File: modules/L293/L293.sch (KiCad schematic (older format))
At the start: 40 parts, among them J1 2, J10 11, J11 12, J12 13, J13 A0, J14 A1, J15 A2, J16 A3, J17 A4, J18 A5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

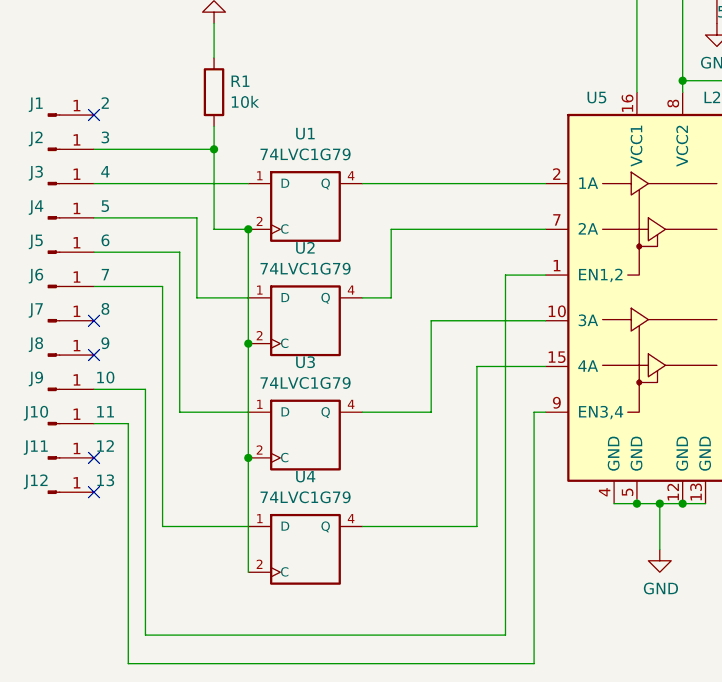
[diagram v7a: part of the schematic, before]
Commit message: Motor shield v2 in work Attention! Pin numbers changed!
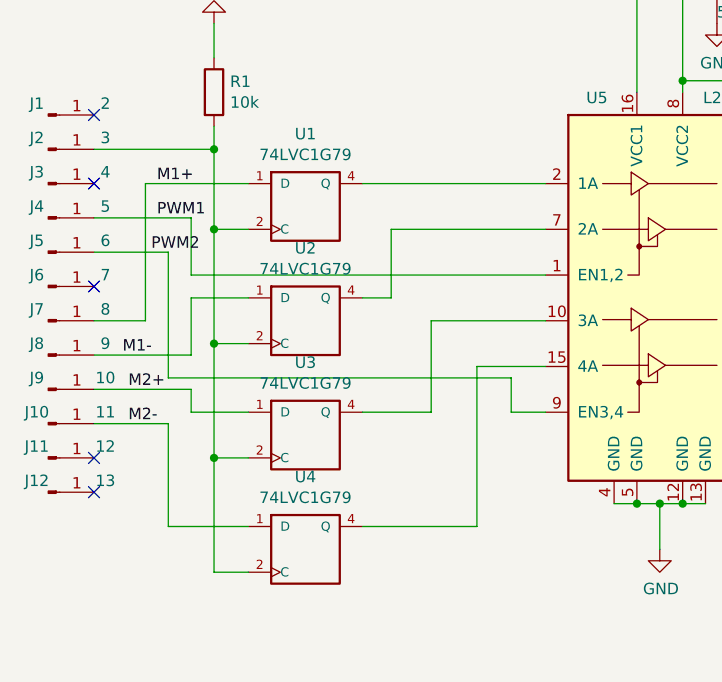
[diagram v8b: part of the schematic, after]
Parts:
- U6: footprint Package_TO_SOT_THT:TO-220-3_Vertical -> Package_TO_SOT_THT:TO-220-3_Horizontal_TabDown
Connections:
- net at J3.1 (Pin_1): no longer U1.1 (D)
- net M1-: now reaches U2.1 (D)
- net M1-: now also J8.1 (Pin_1); no longer J4.1 (Pin_1)
- net M2+: now reaches U3.1 (D)
- net M2+: now also J9.1 (Pin_1); no longer J5.1 (Pin_1)
- net at J6.1 (Pin_1): no longer U4.1 (D)
- net M1+: now reaches J7.1 (Pin_1)
- net M1+: now also U1.1 (D)
- net PWM1: now reaches U5.1 (EN1,2)
- net PWM1: now also J4.1 (Pin_1); no longer J9.1 (Pin_1)
- net M2-: now reaches J10.1 (Pin_1)
- net M2-: now also U4.1 (D); no longer U5.9 (EN3,4)
- new net PWM2: J5.1 (Pin_1), U5.9 (EN3,4)
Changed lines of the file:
@@
 	2900 3600 2900 4300
 Wire Wire Line
-	1225 2800 1900 2800
-Wire Wire Line
-	1225 2950 1675 2950
-Wire Wire Line
-	1675 2950 1675 3300
-Wire Wire Line
-	1675 3300 1900 3300
-Wire Wire Line
-	1225 3100 1600 3100
-Wire Wire Line
-	1600 3100 1600 3800
-Wire Wire Line
-	1600 3800 1900 3800
-Wire Wire Line
-	1225 3250 1525 3250
-Wire Wire Line
-	1525 3250 1525 4300
-Wire Wire Line
-	1525 4300 1900 4300
-Wire Wire Line
-	1900 3000 1900 3500
-Connection ~ 1900 3500
-Connection ~ 1900 4000
-Wire Wire Line
-	1900 3500 1900 4000
-Wire Wire Line
-	1900 4000 1900 4500
-Wire Wire Line
 	1225 2650 1750 2650
 Wire Wire Line
@@
 Wire Wire Line
 	1750 3000 1900 3000
-Connection ~ 1900 3000
-Wire Wire Line
-	1225 3700 1450 3700
-Wire Wire Line
-	1450 3700 1450 4775
-Wire Wire Line
-	1450 4775 3025 4775
-Wire Wire Line
-	3025 4775 3025 3200
-Wire Wire Line
-	3025 3200 3200 3200
-Wire Wire Line
-	1225 3850 1375 3850
-Wire Wire Line
-	1375 3850 1375 4900
-Wire Wire Line
-	1375 4900 3150 4900
-Wire Wire Line
-	3150 4900 3150 3800
-Wire Wire Line
-	3150 3800 3200 3800
 $Comp
 L power:GND #PWR01003
@@
 $EndComp
 NoConn ~ 1225 2500
-NoConn ~ 1225 3400
-NoConn ~ 1225 3550
-NoConn ~ 1225 4000
-NoConn ~ 1225 4150
 NoConn ~ 6750 2500
 NoConn ~ 6750 2650
@@
 F 0 "U6" H 5400 2415 50  0000 C CNN
 F 1 "L4940" H 5400 2324 50  0000 C CNN
-F 2 "Package_TO_SOT_THT:TO-220-3_Vertical" H 5250 2300 50  0001 C CNN
+F 2 "Package_TO_SOT_THT:TO-220-3_Horizontal_TabDown" H 5250 2300 50  0001 C CNN
 F 3 "" H 5250 2300 50  0001 C CNN
 	1    5400 2250
@@
 Wire Wire Line
 	3600 1750 3600 2400
+Wire Wire Line
+	1225 2950 1650 2950
+Wire Wire Line
+	1650 2950 1650 3200
+Wire Wire Line
+	1650 3200 3200 3200
+Wire Wire Line
+	1225 3100 1550 3100
+Wire Wire Line
+	1550 3100 1550 3650
+Wire Wire Line
+	1550 3650 3050 3650
+Wire Wire Line
+	3050 3650 3050 3800
+Wire Wire Line
+	3050 3800 3200 3800
+Wire Wire Line
+	1225 3550 1650 3550
+Wire Wire Line
+	1650 3550 1650 3300
+Wire Wire Line
+	1650 3300 1900 3300
+Wire Wire Line
+	1225 3400 1450 3400
+Wire Wire Line
+	1450 3400 1450 2800
+Wire Wire Line
+	1450 2800 1900 2800
+Wire Wire Line
+	1225 3700 1650 3700
+Wire Wire Line
+	1650 3700 1650 3800
+Wire Wire Line
+	1650 3800 1900 3800
+Wire Wire Line
+	1225 3850 1550 3850
+Wire Wire Line
+	1550 3850 1550 4300
+Wire Wire Line
+	1550 4300 1900 4300
+Wire Wire Line
+	1750 3000 1750 3500
+Wire Wire Line
+	1750 3500 1900 3500
+Connection ~ 1750 3000
+Wire Wire Line
+	1750 3500 1750 4000
+Wire Wire Line
+	1750 4000 1900 4000
+Connection ~ 1750 3500
+Wire Wire Line
+	1750 4000 1750 4500
+Wire Wire Line
+	1750 4500 1900 4500
+Connection ~ 1750 4000
+Text Label 1500 2950 0    50   ~ 0
+PWM1
+Text Label 1475 3100 0    50   ~ 0
+PWM2
+Text Label 1500 2800 0    50   ~ 0
+M1+
+Text Label 1350 3550 0    50   ~ 0
+M1-
+Text Label 1375 3700 0    50   ~ 0
+M2+
+Text Label 1375 3850 0    50   ~ 0
+M2-
+NoConn ~ 1225 2800
+NoConn ~ 1225 3250
+NoConn ~ 1225 4000
+NoConn ~ 1225 4150
 $EndSCHEMATC
